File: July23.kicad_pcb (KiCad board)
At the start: 2 copper layers, 109.5 x 74 mm, 67 parts, among them P1 12v In, P2 HeatOut, P3 LED, P4 Temp1, P5 Temp2, P6 Temp3, P7 ExtPwr, Q1 SFH3711, Q10 SFH3711, Q11 SFH3711, Q12 SFH3711, Q13 SFH3711, Q14 SFH3711, Q15 SFH3711, Q16 Q_NMOS_GSD, Q17 Q_NMOS_GSD, Q2 SFH3711, Q3 SFH3711, Q4 SFH3711, Q5 SFH3711, Q6 SFH3711, Q7 SFH3711, Q8 SFH3711, Q9 SFH3711, U1 Teensy_3.1, U2 LM358, U3 CD74HC4067, U4 MC78M05CDT, U5 NCR405U

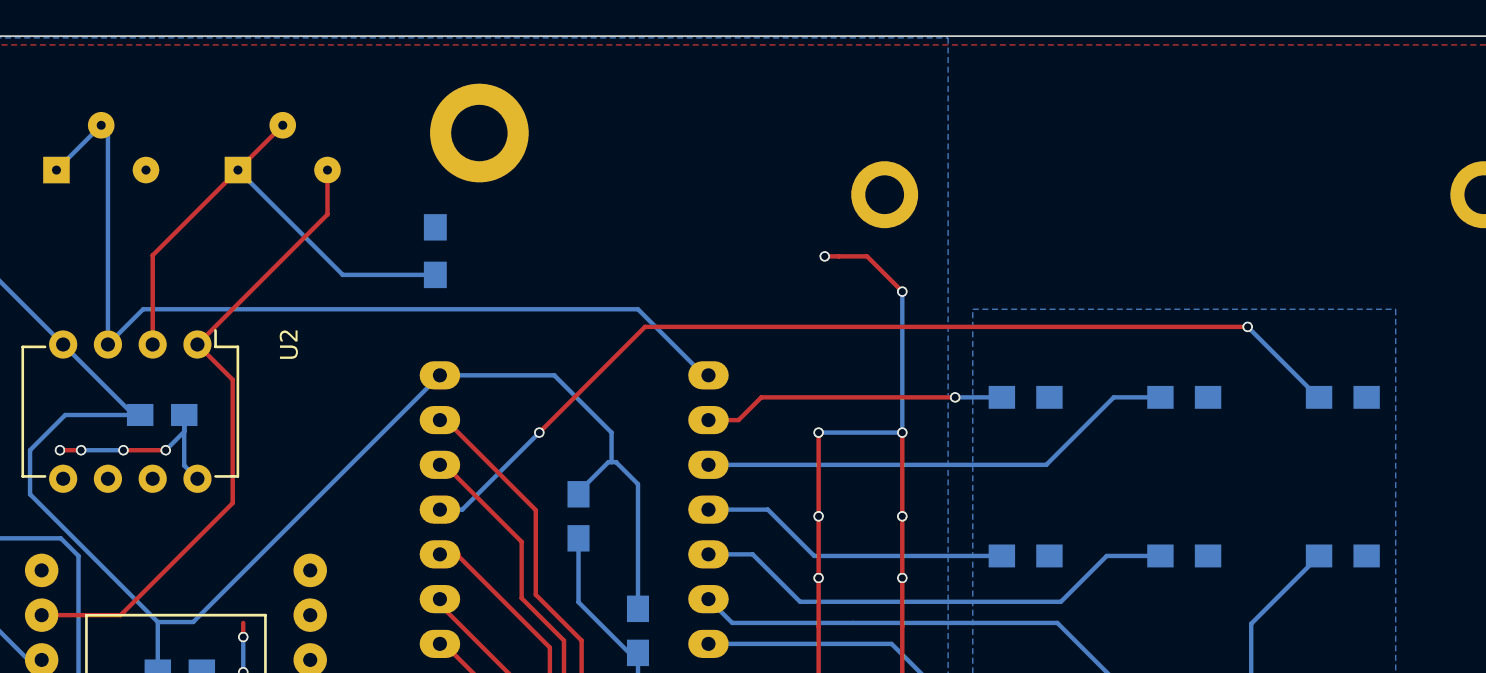
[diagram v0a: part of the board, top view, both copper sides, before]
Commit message: Changed schematic of SFH3710
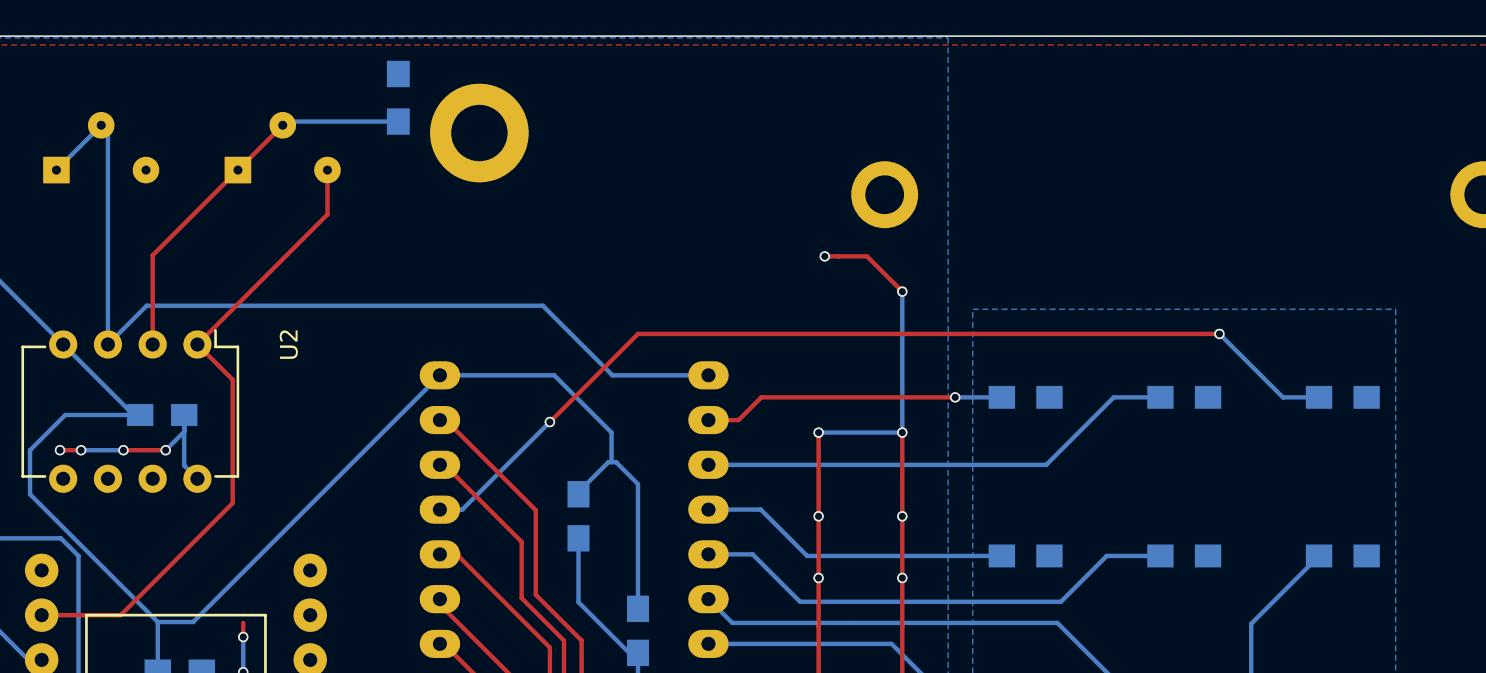
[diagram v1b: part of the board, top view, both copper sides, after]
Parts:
- Q1, Q10, Q11, Q12, Q13, Q14, Q15, Q2, Q3, Q4, Q5, Q6, Q7, Q8, Q9: value SFH3711 -> SFH3710
- moved R1 8.95 mm to (181.4, 56.0)
- turned Q11 to 0 degrees
- turned Q6 to 0 degrees
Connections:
- Q11 pad 1: +3V3 -> /Phototransistors/S11
- Q11 pad 2: /Phototransistors/S11 -> +3V3
- Q6 pad 1: +3V3 -> /Phototransistors/S6
- Q6 pad 2: /Phototransistors/S6 -> +3V3
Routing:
- net Net-(R1-Pad1): track 29.8 -> 22.8 mm

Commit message: OpAmp circuit needs checking
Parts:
- R3, R4, R5: value R -> R330
- RV1: value POT 10k -> 10k
- RV2: value POT -> 10k
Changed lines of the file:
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@@
       (effects (font (size 1 1) (thickness 0.15)) (justify mirror))
     )
-    (fp_text value R (at 0 -2.1) (layer B.Fab)
+    (fp_text value R330 (at 0 -2.1) (layer B.Fab)
       (effects (font (size 1 1) (thickness 0.15)) (justify mirror))
     )
@@
       (effects (font (size 1 1) (thickness 0.15)) (justify mirror))
     )
-    (fp_text value R (at 0 -2.1) (layer B.Fab)
+    (fp_text value R330 (at 0 -2.1) (layer B.Fab)
       (effects (font (size 1 1) (thickness 0.15)) (justify mirror))
     )
@@
       (effects (font (size 1 1) (thickness 0.15)) (justify mirror))
     )
-    (fp_text value R (at 0 -2.1) (layer B.Fab)
+    (fp_text value R330 (at 0 -2.1) (layer B.Fab)
       (effects (font (size 1 1) (thickness 0.15)) (justify mirror))
     )
@@
       (effects (font (size 1 1) (thickness 0.15)) (justify mirror))
     )
-    (fp_text value "POT 10k" (at 2.54 -6.096) (layer B.Fab)
+    (fp_text value 10k (at 2.54 -6.096) (layer B.Fab)
       (effects (font (size 1 1) (thickness 0.15)) (justify mirror))
     )
@@
       (effects (font (size 1 1) (thickness 0.15)) (justify mirror))
     )
-    (fp_text value POT (at 2.54 -6.096) (layer B.Fab)
+    (fp_text value 10k (at 2.54 -6.096) (layer B.Fab)
       (effects (font (size 1 1) (thickness 0.15)) (justify mirror))
     )
@@
   (segment (start 183.76 76.83) (end 184.23 76.83) (width 0.25) (layer B.Cu) (net 15))
   (segment (start 183.76 76.83) (end 184.17 76.83) (width 0.25) (layer F.Cu) (net 15))
-  (segment (start 183.76 79.37) (end 185.03 79.37) (width 0.25) (layer B.Cu) (net 16) (status 400000))
-  (segment (start 231.6 73) (end 233.65 73) (width 0.25) (layer B.Cu) (net 16) (status 800000))
+  (segment (start 183.76 79.37) (end 185.03 79.37) (width 0.25) (layer B.Cu) (net 16))
+  (segment (start 231.6 73) (end 233.65 73) (width 0.25) (layer B.Cu) (net 16))
   (segment (start 228 69.4) (end 231.6 73) (width 0.25) (layer B.Cu) (net 16))
   (via (at 228 69.4) (size 0.6) (drill 0.4) (layers F.Cu B.Cu) (net 16))
@@
   (segment (start 158.9 100.6) (end 161.16 100.6) (width 0.25) (layer B.Cu) (net 21))
   (segment (start 157.1 102.4) (end 158.9 100.6) (width 0.25) (layer B.Cu) (net 21))
-  (segment (start 181.4 57.35) (end 175.05 57.35) (width 0.25) (layer B.Cu) (net 22) (status C00000))
-  (segment (start 175.05 57.35) (end 174.84 57.56) (width 0.25) (layer B.Cu) (net 22) (status C00000))
+  (segment (start 181.4 57.35) (end 175.05 57.35) (width 0.25) (layer B.Cu) (net 22))
+  (segment (start 175.05 57.35) (end 174.84 57.56) (width 0.25) (layer B.Cu) (net 22))
   (segment (start 172.3 60.1) (end 174.84 57.56) (width 0.25) (layer F.Cu) (net 22))
   (segment (start 167.46 70) (end 167.46 64.94) (width 0.25) (layer F.Cu) (net 22))
@@
   (segment (start 165.64 85.36) (end 172 79) (width 0.25) (layer F.Cu) (net 23))
   (segment (start 169.53 69.53) (end 170 70) (width 0.25) (layer F.Cu) (net 23))
-  (segment (start 199 71.75) (end 193.55 71.75) (width 0.25) (layer B.Cu) (net 24) (status 400000))
-  (segment (start 167.12 67.8) (end 164.92 70) (width 0.25) (layer B.Cu) (net 24) (status 800000))
+  (segment (start 199 71.75) (end 193.55 71.75) (width 0.25) (layer B.Cu) (net 24))
+  (segment (start 167.12 67.8) (end 164.92 70) (width 0.25) (layer B.Cu) (net 24))
   (segment (start 189.6 67.8) (end 167.12 67.8) (width 0.25) (layer B.Cu) (net 24))
   (segment (start 193.55 71.75) (end 189.6 67.8) (width 0.25) (layer B.Cu) (net 24))

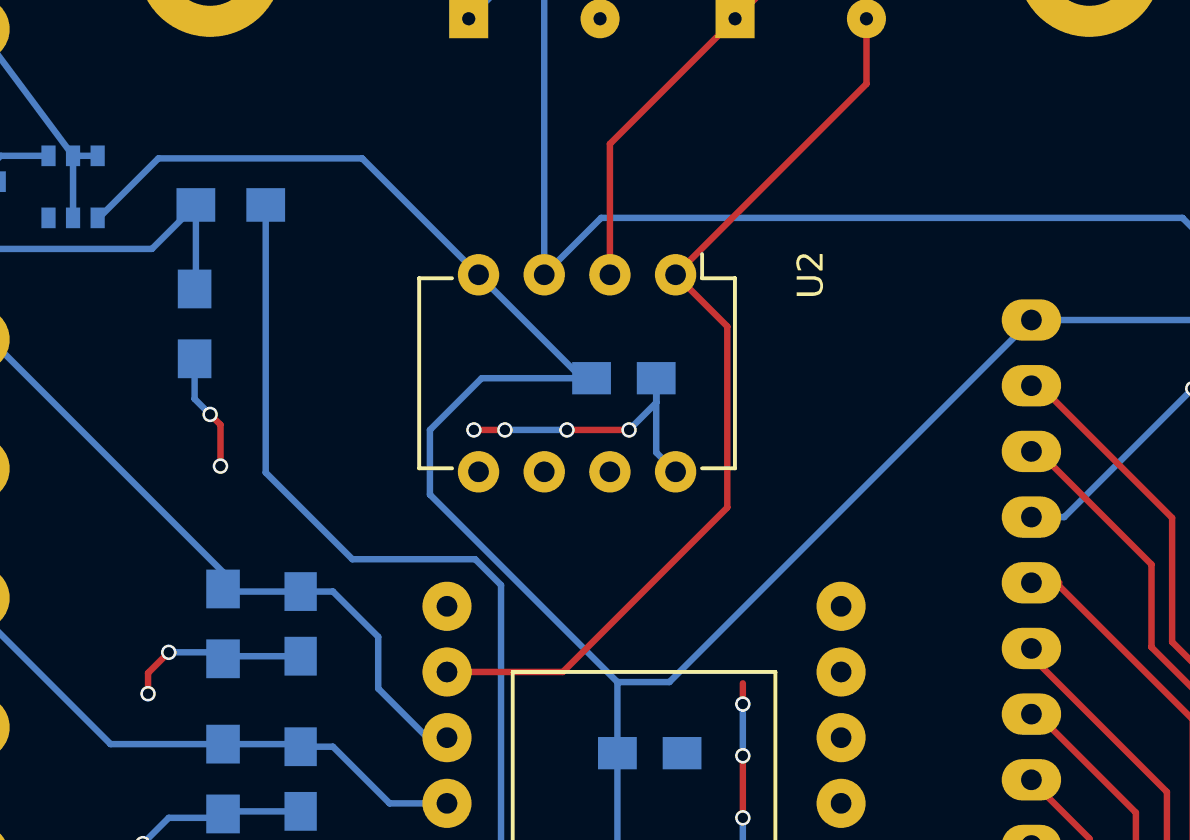
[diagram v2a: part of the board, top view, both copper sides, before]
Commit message: fixing up opamp on PCB (work in progress)
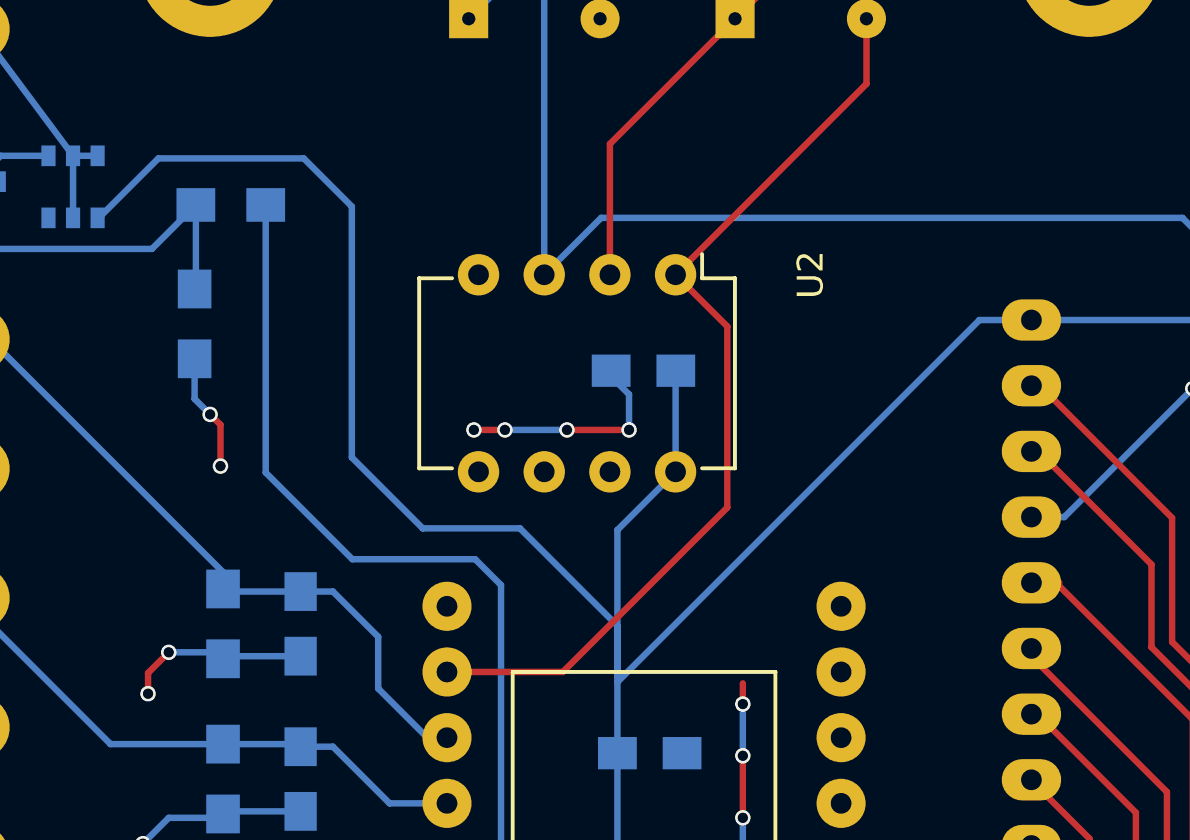
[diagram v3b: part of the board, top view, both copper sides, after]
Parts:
- moved C2 0.81 mm to (168.8, 73.7), turned to 180 degrees
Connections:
- net Net-(R1-Pad1) renamed /Amp-
- net Net-(RV1-Pad3) renamed /Amp_Out
- net Net-(RV2-Pad1) renamed /Amp+
- U2 pad 4: +3V3 -> GND
- U2 pad 8: GND -> +3V3
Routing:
- net +3V3: track 254.4 -> 260.2 mm
- net GND: track 253.0 -> 249.0 mm

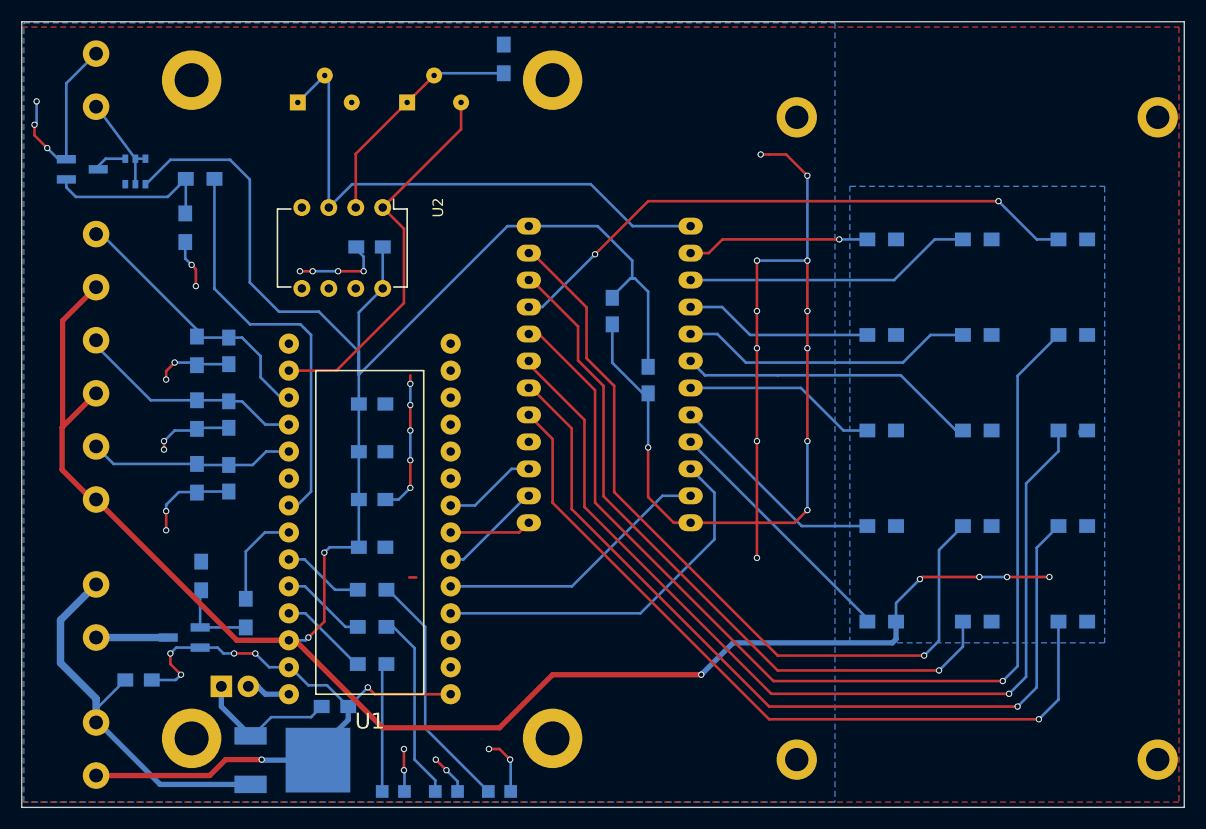
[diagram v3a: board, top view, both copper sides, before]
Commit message: improved Gnd stitching
unused part of LM358 still to be connected somewhere
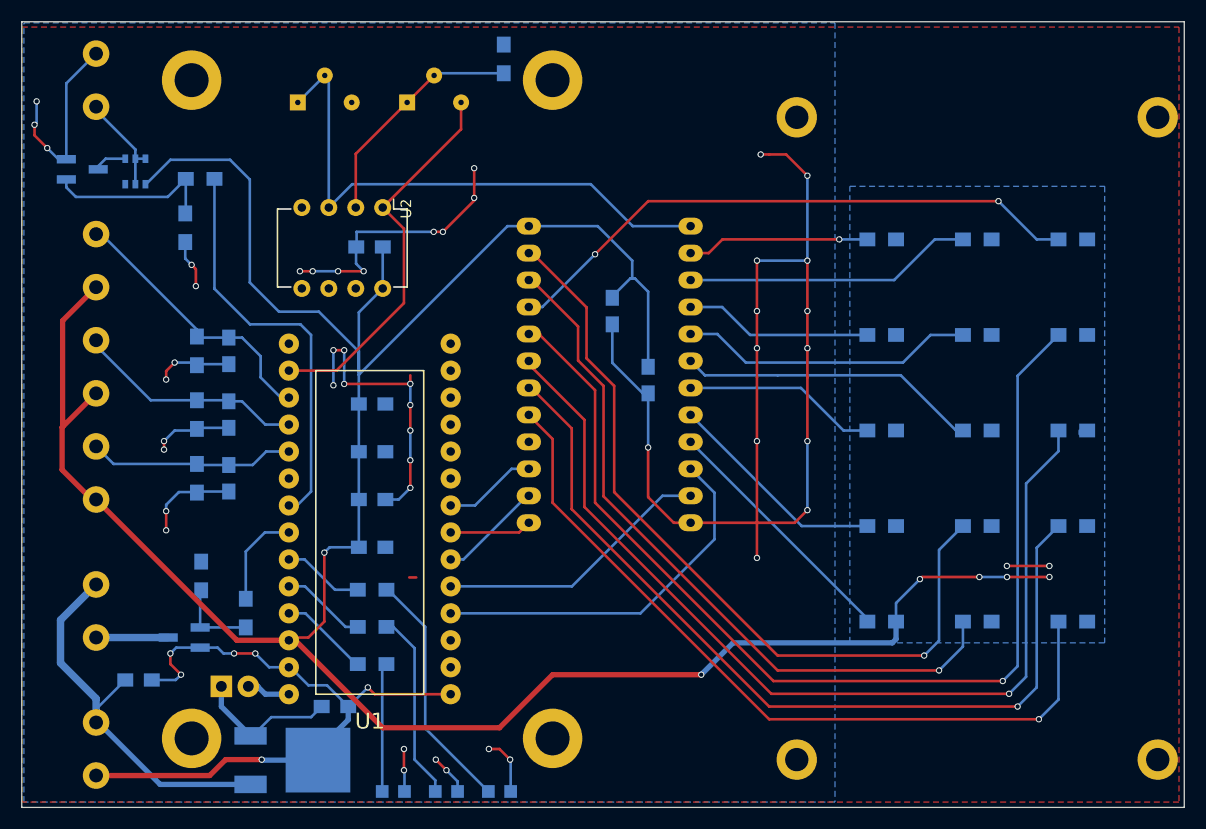
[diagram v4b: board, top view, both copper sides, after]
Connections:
- U2 pad 5: (no net) -> Net-(U2-Pad5)
- U2 pad 6: (no net) -> Net-(U2-Pad6)
- U2 pad 7: (no net) -> Net-(U2-Pad6)
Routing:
- net GND: track 249.0 -> 279.8 mm, vias 45 -> 53
- net (no net): track 0.66 -> 4.66 mm, vias 0 -> 2
- net +3V3: vias 7 -> 6
